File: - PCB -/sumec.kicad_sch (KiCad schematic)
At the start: 31 parts, among them IC1 XT30U-F, J1 Conn_01x05_Pin, J2 Conn_01x05_Pin, J3 Conn_01x05_Pin, J4 Conn_01x05_Male, J5 Conn_01x03_Male, J6 Screw_Terminal_01x03, J7 Screw_Terminal_01x03, J8 Screw_Terminal_01x03, J9 Screw_Terminal_01x03, SW1 SW_SPDT, U10 VL53L0X, U11 LD1086V33-DG, U5 TSOP382xx, U7 ROB-14450, U8 VL53L0X, U9 VL53L0X

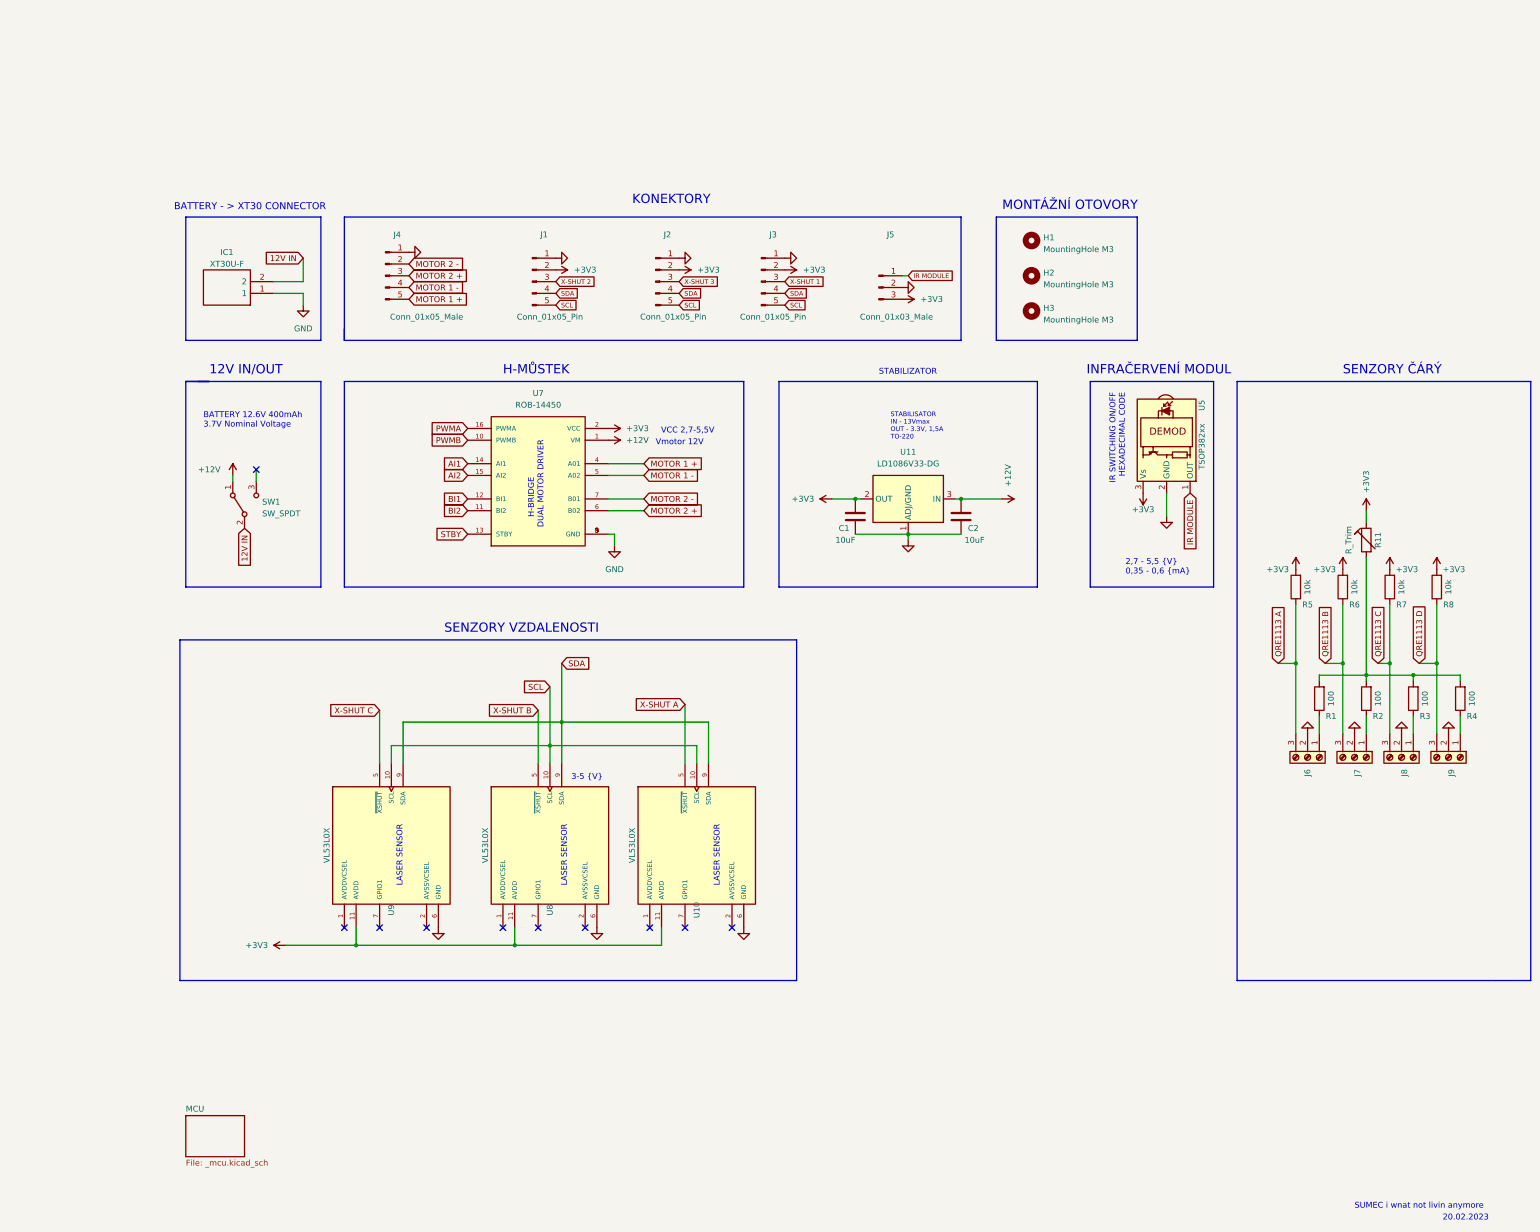
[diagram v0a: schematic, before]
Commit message: PCB and DOCS update: Page structure (WIP) and BOM
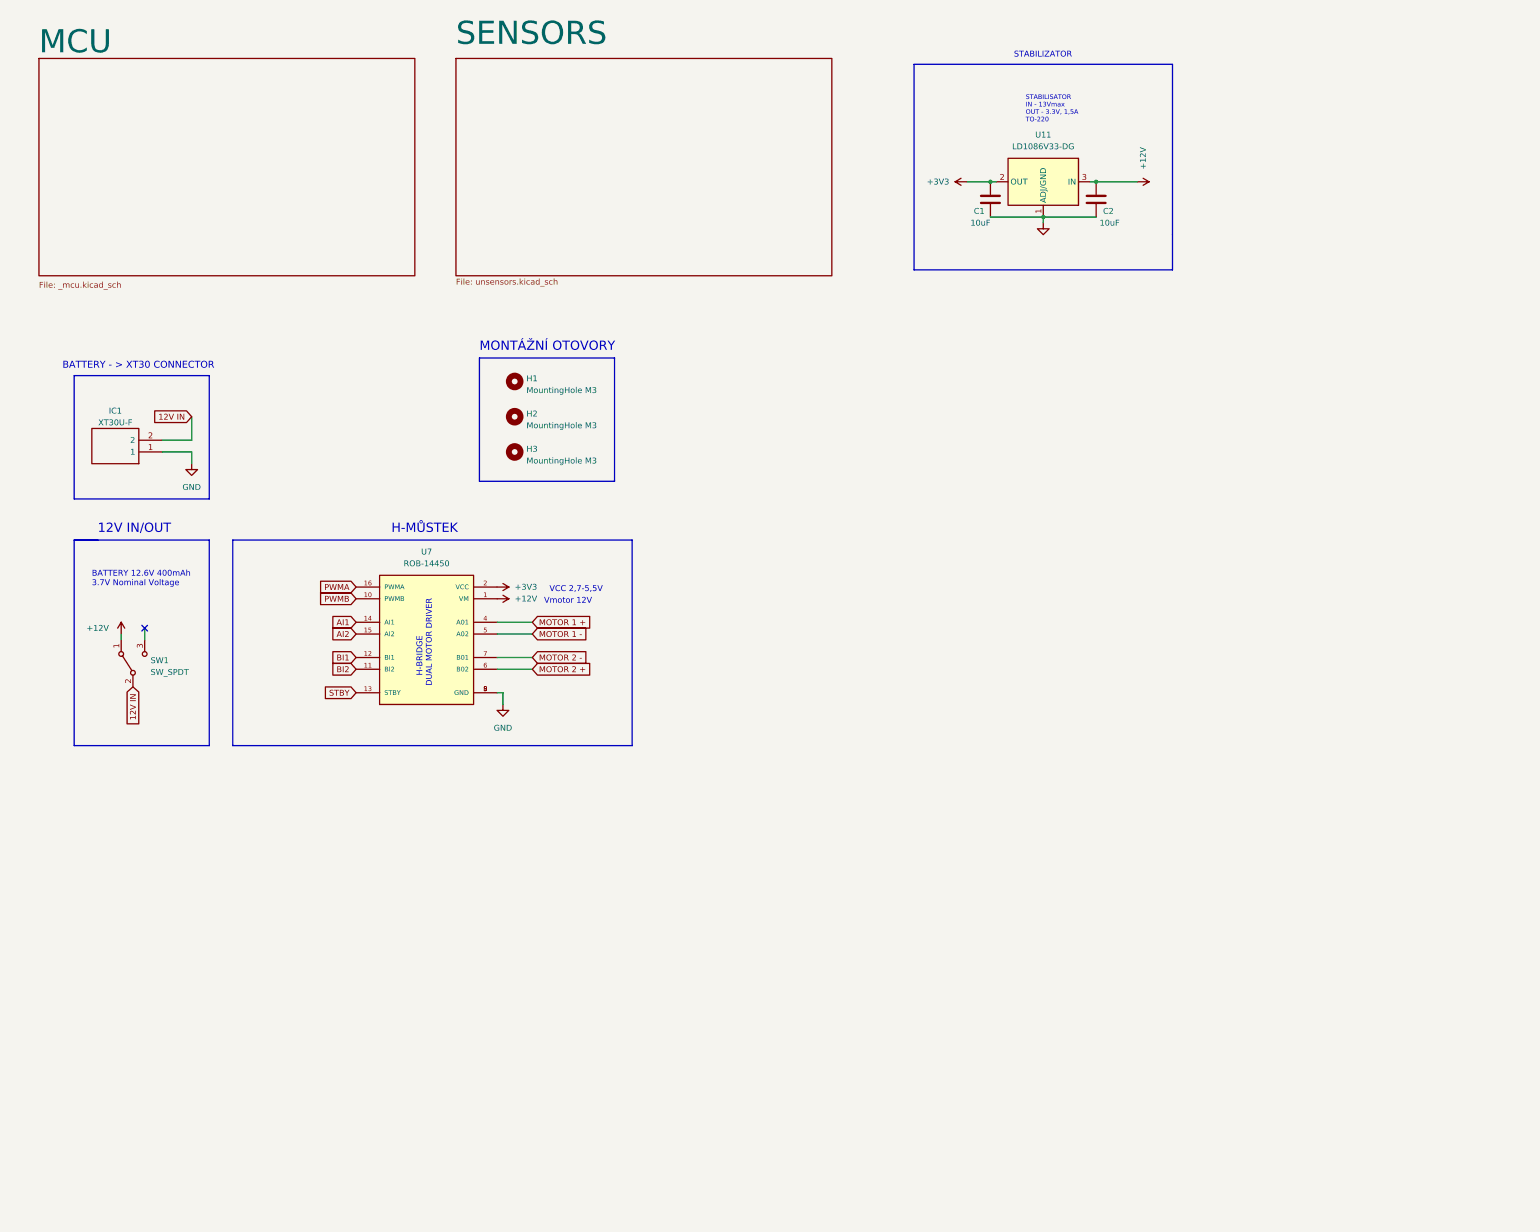
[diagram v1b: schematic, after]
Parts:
- removed J1, J2, J3: Conn_01x05_Pin, Connector_PinSocket_2.54mm:PinSocket_1x05_P2.54mm_Vertical, symbol Connector:Conn_01x05_Pin
- removed J4: Conn_01x05_Male, Connector_PinSocket_2.54mm:PinSocket_1x05_P2.54mm_Vertical, symbol Connector:Conn_01x05_Male
- removed J5: Conn_01x03_Male, Connector_PinSocket_2.54mm:PinSocket_1x03_P2.54mm_Vertical, symbol Connector:Conn_01x03_Male
- removed J6, J7, J8, J9: Screw_Terminal_01x03, TerminalBlock:TerminalBlock_bornier-3_P5.08mm, symbol Connector:Screw_Terminal_01x03
- removed R1, R2, R3, R4: 100, Resistor_THT:R_Axial_DIN0207_L6.3mm_D2.5mm_P10.16mm_Horizontal, symbol Device:R
- removed R11: R_Trim, Potentiometer_THT:Potentiometer_ACP_CA9-V10_Vertical, symbol Device:R_Trim
- removed R5, R6, R7, R8: 10k, Resistor_THT:R_Axial_DIN0207_L6.3mm_D2.5mm_P10.16mm_Horizontal, symbol Device:R
- removed U10, U8, U9: VL53L0X, SENSOR_VL53L0X, symbol VL53L0X:VL53L0X
- removed U5: TSOP382xx, OptoDevice:Vishay_MINICAST-3Pin, symbol Interface_Optical:TSOP382xx
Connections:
- no-connect marks 10 -> 1
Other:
- added sheet SENSORS (unsensors.kicad_sch)
- note removed: "2,7 - 5,5 {V} 0,35 - 0,6 {mA}"
- note removed: "20.02.2023"
- note removed: "3-5 {V}"
- note removed: "INFRAČERVENÍ MODUL"
- note removed: "IR SWITCHING ON/OFF HEXADECIMAL CODE"
- note removed: "KONEKTORY"
- note removed: "LASER SENSOR"
- note removed: "SENZORY VZDALENOSTI"
- note removed: "SENZORY ČÁRÝ"
- note removed: "SUMEC i wnat not livin anymore"
- moved on the sheet: C1, C2, H1, H2, H3, IC1, SW1, U11, U7

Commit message: SCH WIP UPDATE
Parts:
- removed C1, C2: 10uF, Capacitor_THT:CP_Radial_D4.0mm_P2.00mm, symbol Device:C
- removed H1, H2, H3: MountingHole M3, MountingHole:MountingHole_3.2mm_M3, symbol Mechanical:MountingHole
- removed IC1: XT30U-F, Connector_AMASS:AMASS_XT30U-M_1x02_P5.0mm_Vertical, symbol SamacSys_Parts:XT30U-M
- removed SW1: SW_SPDT, SWITCH:SW_100SP1T1B4M2QE, symbol Switch:SW_SPDT
- removed U11: LD1086V33-DG, Package_TO_SOT_THT:TO-220-3_Vertical, symbol Regulator_Linear:LD1086V33-DG
- removed U7: ROB-14450, H-BRIDGE:MODULE_ROB-14450, symbol ROB-14450:ROB-14450
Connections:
- no-connect marks 1 -> 0
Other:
- added sheet MECHANICS (MECHANICS.kicad_sch)
- added sheet POWER SUPPLY (POWER SUPPLY.kicad_sch)
- sheet MCU: file _mcu.kicad_sch -> MCU.kicad_sch
- sheet SENSORS: file unsensors.kicad_sch -> SENSORS.kicad_sch
- note removed: "12V IN/OUT"
- note removed: "BATTERY - > XT30 CONNECTOR"
- note removed: "BATTERY 12.6V 400mAh 3.7V Nominal Voltage"
- note removed: "H-BRIDGE DUAL MOTOR DRIVER"
- note removed: "H-MŮSTEK"
- note removed: "MONTÁŽNÍ OTOVORY"
- note removed: "STABILISATOR IN - 13Vmax OUT - 3.3V, 1,5A TO-220"
- note removed: "STABILIZATOR"
- note removed: "VCC 2,7-5,5V"
- note removed: "Vmotor 12V"

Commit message: PCB sumec THT update
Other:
- company: (none) -> SPŠ NA PROSEKU
- title: (none) -> SUMEC THT
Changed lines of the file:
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@@
 (kicad_sch (version 20230121) (generator eeschema)
   (paper "A4")
+  (title_block
+    (title "SUMEC THT")
+    (company "SPŠ NA PROSEKU")
+  )
   (sheet (at 21.59 83.82) (size 69.85 46.99)
     (stroke (width 0.1524) (type solid) (color 0 0 0 1))
